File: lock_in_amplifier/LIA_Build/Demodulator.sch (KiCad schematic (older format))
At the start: 22 parts, among them J34 DEMOD PROG, J39 BOOT, J42 VOCM, J45 rst, J48 XOUT, U11 ADA2200, U5 LM833

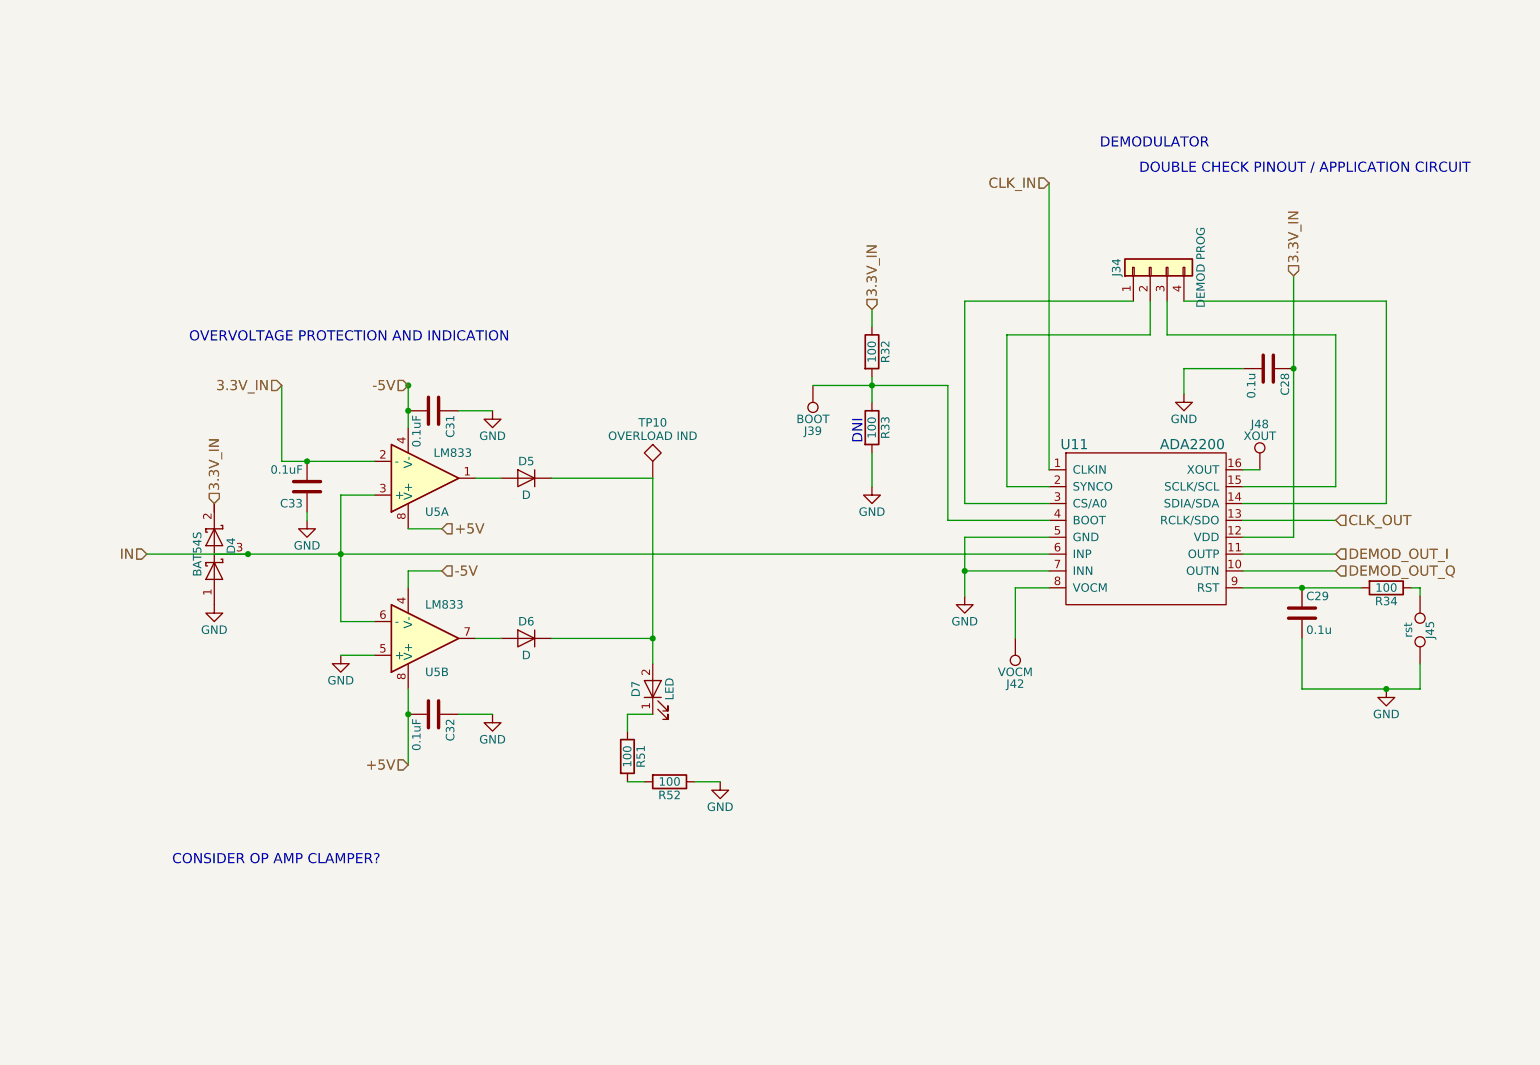
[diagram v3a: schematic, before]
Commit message: PLL initial implementation
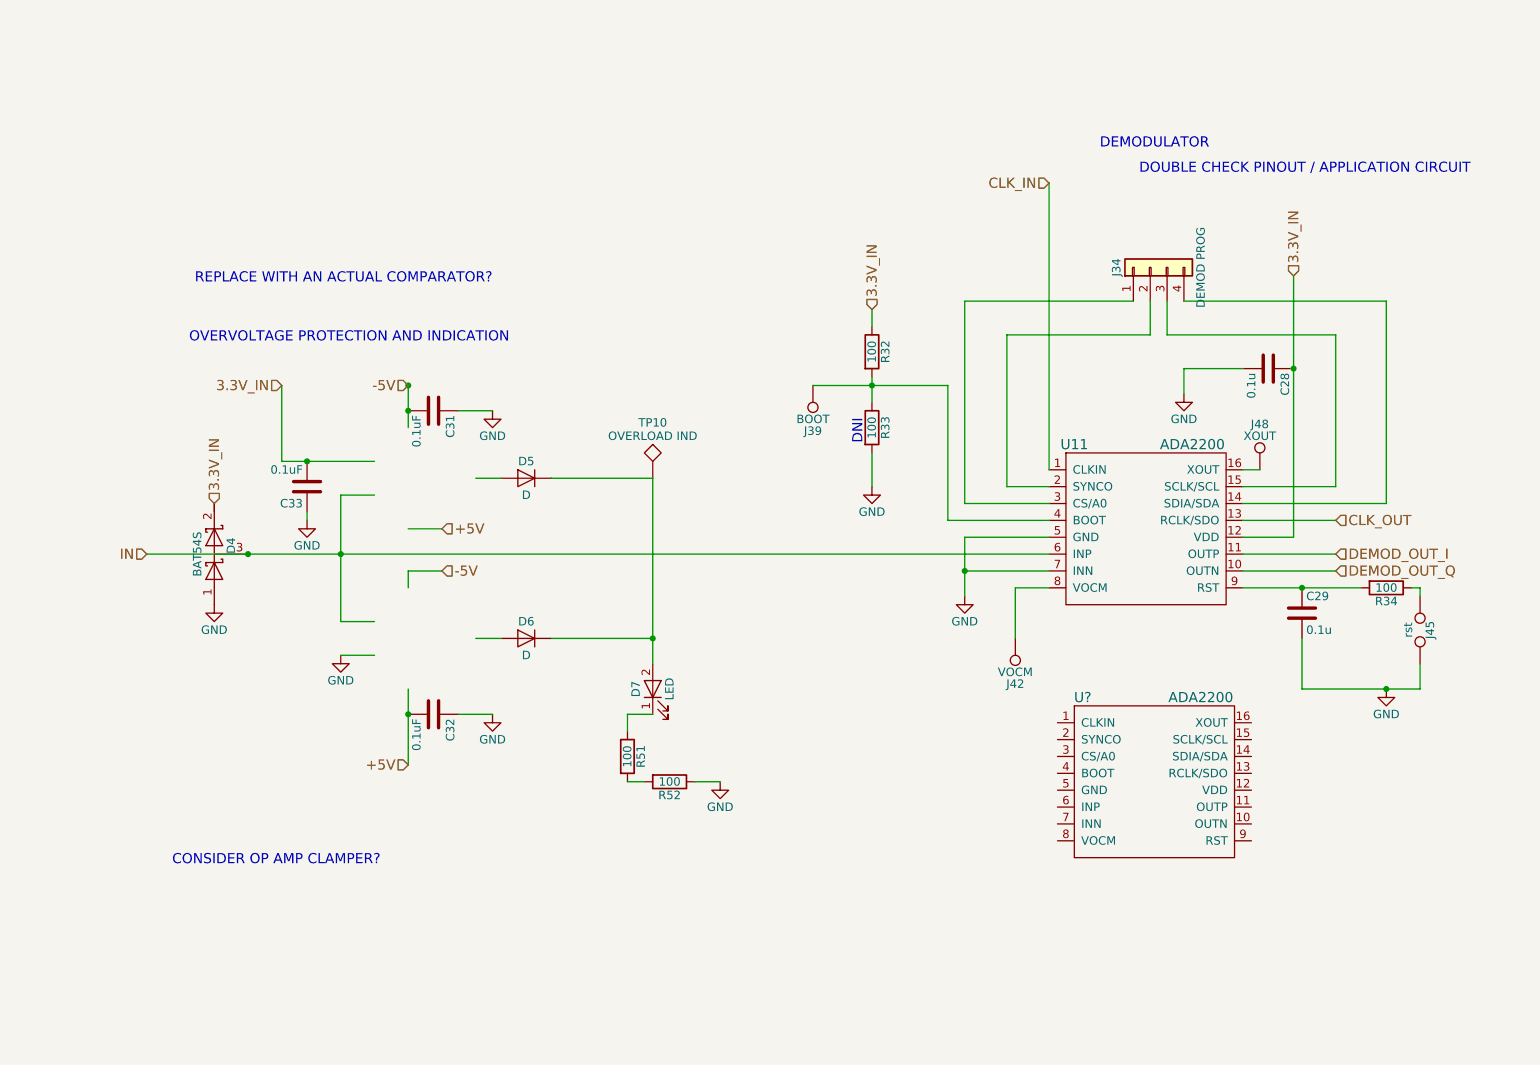
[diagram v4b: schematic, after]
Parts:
- removed U5: LM833, symbol LM358
- added U?: ADA2200, Housings_SSOP:TSSOP-20_4.4x6.5mm_Pitch0.65mm, symbol ADA2200
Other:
- note added: "REPLACE WITH AN ACTUAL COMPARATOR?"
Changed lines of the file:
@@
 $EndComp
 $Comp
-L GND #PWR045
+L GND #PWR50
 U 1 1 5A22E931
 P 6150 4200
-F 0 "#PWR045" H 6150 3950 50  0001 C CNN
+F 0 "#PWR50" H 6150 3950 50  0001 C CNN
 F 1 "GND" H 6150 4050 50  0000 C CNN
 F 2 "" H 6150 4200 50  0001 C CNN
@@
 $EndComp
 $Comp
-L GND #PWR046
+L GND #PWR51
 U 1 1 5A22EB23
 P 7450 3000
-F 0 "#PWR046" H 7450 2750 50  0001 C CNN
+F 0 "#PWR51" H 7450 2750 50  0001 C CNN
 F 1 "GND" H 7450 2850 50  0000 C CNN
 F 2 "" H 7450 3000 50  0001 C CNN
@@
 $EndComp
 $Comp
-L GND #PWR047
+L GND #PWR52
 U 1 1 5A22F9DC
 P 8650 4750
-F 0 "#PWR047" H 8650 4500 50  0001 C CNN
+F 0 "#PWR52" H 8650 4500 50  0001 C CNN
 F 1 "GND" H 8650 4600 50  0000 C CNN
 F 2 "" H 8650 4750 50  0001 C CNN
@@
 $EndComp
 $Comp
-L GND #PWR048
+L GND #PWR49
 U 1 1 5A22FE7B
 P 5600 3550
-F 0 "#PWR048" H 5600 3300 50  0001 C CNN
+F 0 "#PWR49" H 5600 3300 50  0001 C CNN
 F 1 "GND" H 5600 3400 50  0000 C CNN
 F 2 "" H 5600 3550 50  0001 C CNN
@@
 $EndComp
 $Comp
-L GND #PWR049
+L GND #PWR43
 U 1 1 5A231A02
 P 1700 4250
-F 0 "#PWR049" H 1700 4000 50  0001 C CNN
+F 0 "#PWR43" H 1700 4000 50  0001 C CNN
 F 1 "GND" H 1700 4100 50  0000 C CNN
 F 2 "" H 1700 4250 50  0001 C CNN
@@
 	0    -1   -1   0
 $EndComp
-$Comp
-L LM358 U5
-U 1 1 5A210395
-P 2950 3500
-F 0 "U5" H 2950 3700 50  0000 L CNN
-F 1 "LM833" H 3000 3350 50  0000 L CNN
-F 2 "" H 2950 3500 50  0001 C CNN
-F 3 "" H 2950 3500 50  0001 C CNN
-	1    2950 3500
-	1    0    0    1
-$EndComp
-$Comp
-L LM358 U5
-U 2 1 5A2103E8
-P 2950 4450
-F 0 "U5" H 2950 4650 50  0000 L CNN
-F 1 "LM833" H 2950 4250 50  0000 L CNN
-F 2 "" H 2950 4450 50  0001 C CNN
-F 3 "" H 2950 4450 50  0001 C CNN
-	2    2950 4450
-	1    0    0    1
-$EndComp
 Text HLabel 2100 2950 0    60   Input ~ 0
 3.3V_IN
 $Comp
-L GND #PWR050
+L GND #PWR45
 U 1 1 5A21049D
 P 2450 4550
-F 0 "#PWR050" H 2450 4300 50  0001 C CNN
+F 0 "#PWR45" H 2450 4300 50  0001 C CNN
 F 1 "GND" H 2450 4400 50  0000 C CNN
 F 2 "" H 2450 4550 50  0001 C CNN
@@
 Connection ~ 2450 3950
 $Comp
-L GND #PWR051
+L GND #PWR48
 U 1 1 5A2108F7
 P 4700 5300
-F 0 "#PWR051" H 4700 5050 50  0001 C CNN
+F 0 "#PWR48" H 4700 5050 50  0001 C CNN
 F 1 "GND" H 4700 5150 50  0000 C CNN
 F 2 "" H 4700 5300 50  0001 C CNN
@@
 $EndComp
 $Comp
-L GND #PWR052
+L GND #PWR46
 U 1 1 5A210C1D
 P 3350 3100
-F 0 "#PWR052" H 3350 2850 50  0001 C CNN
+F 0 "#PWR46" H 3350 2850 50  0001 C CNN
 F 1 "GND" H 3350 2950 50  0000 C CNN
 F 2 "" H 3350 3100 50  0001 C CNN
@@
 Connection ~ 2850 4900
 $Comp
-L GND #PWR053
+L GND #PWR47
 U 1 1 5A2111CA
 P 3350 4900
-F 0 "#PWR053" H 3350 4650 50  0001 C CNN
+F 0 "#PWR47" H 3350 4650 50  0001 C CNN
 F 1 "GND" H 3350 4750 50  0000 C CNN
 F 2 "" H 3350 4900 50  0001 C CNN
@@
 $EndComp
 $Comp
-L GND #PWR054
+L GND #PWR44
 U 1 1 5A214FCE
 P 2250 3750
-F 0 "#PWR054" H 2250 3500 50  0001 C CNN
+F 0 "#PWR44" H 2250 3500 50  0001 C CNN
 F 1 "GND" H 2250 3600 50  0000 C CNN
 F 2 "" H 2250 3750 50  0001 C CNN
@@
 Text Notes 1450 5800 0    60   ~ 0
 CONSIDER OP AMP CLAMPER?
+Text Notes 3350 2350 2    60   ~ 0
+REPLACE WITH AN ACTUAL COMPARATOR?
+$Comp
+L ADA2200 U?
+U 1 1 5A2936CF
+P 7250 5300
+F 0 "U?" H 6850 5800 60  0000 C CNN
+F 1 "ADA2200" H 7550 5800 60  0000 C CNN
+F 2 "Housings_SSOP:TSSOP-20_4.4x6.5mm_Pitch0.65mm" H 7150 5500 60  0001 C CNN
+F 3 "" H 7150 5500 60  0001 C CNN
+	1    7250 5300
+	1    0    0    -1
+$EndComp
 $EndSCHEMATC

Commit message: Added quadrature demod, phase shift to pll
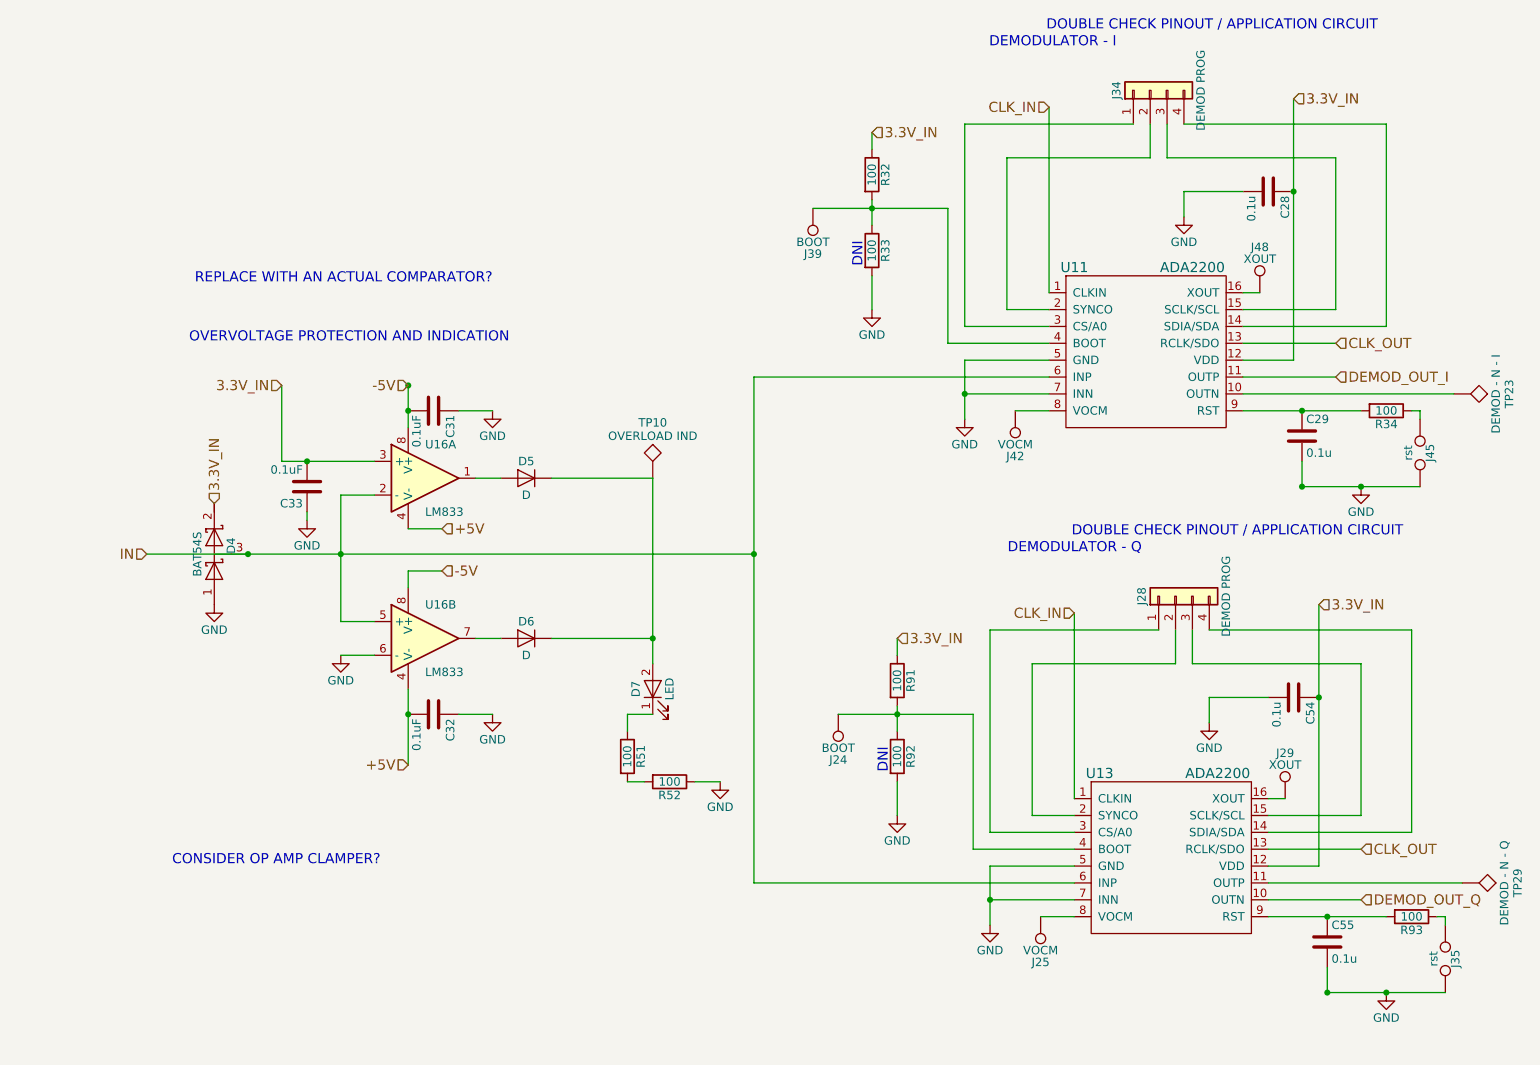
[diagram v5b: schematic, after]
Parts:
- removed U?: ADA2200, Housings_SSOP:TSSOP-20_4.4x6.5mm_Pitch0.65mm, symbol ADA2200
- added C54, C55: 0.1u, Capacitors_SMD:C_0805, symbol C
- added J24: BOOT, footprints:tyco_RCU_0603_Probe_Pad, symbol TEST_1P
- added J25: VOCM, footprints:tyco_RCU_0603_Probe_Pad, symbol TEST_1P
- added J28: DEMOD PROG, Pin_Headers:Pin_Header_Straight_1x04_Pitch2.54mm, symbol Conn_01x04
- added J29: XOUT, footprints:tyco_RCU_0603_Probe_Pad, symbol TEST_1P
- added J35: rst, symbol TEST_2P
- added R91, R92, R93: 100, Resistors_SMD:R_0805, symbol R
- added TP23: DEMOD - N - I, symbol TEST
- added TP29: DEMOD - N - Q, symbol TEST
- added U13: ADA2200, Housings_SSOP:TSSOP-20_4.4x6.5mm_Pitch0.65mm, symbol ADA2200
- added U16: LM833, symbol LM833
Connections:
- wire segments 64 -> 103
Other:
- note added: "DEMODULATOR - I"
- note added: "DEMODULATOR - Q"
- note removed: "DEMODULATOR"
- moved on the sheet: C28, C29, J34, J39, J42, J45, J48, R32, R33, R34, U11

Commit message: pll finalized - misc cleanup - review candidate
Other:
- note removed: "CONSIDER OP AMP CLAMPER?"
- note removed: "REPLACE WITH AN ACTUAL COMPARATOR?"
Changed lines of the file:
@@
 $EndComp
 $Comp
-L GND #PWR045
+L GND #PWR050
 U 1 1 5A22E931
 P 6150 3150
-F 0 "#PWR045" H 6150 2900 50  0001 C CNN
+F 0 "#PWR050" H 6150 2900 50  0001 C CNN
 F 1 "GND" H 6150 3000 50  0000 C CNN
 F 2 "" H 6150 3150 50  0001 C CNN
@@
 $EndComp
 $Comp
-L GND #PWR046
+L GND #PWR051
 U 1 1 5A22EB23
 P 7450 1950
-F 0 "#PWR046" H 7450 1700 50  0001 C CNN
+F 0 "#PWR051" H 7450 1700 50  0001 C CNN
 F 1 "GND" H 7450 1800 50  0000 C CNN
 F 2 "" H 7450 1950 50  0001 C CNN
@@
 $EndComp
 $Comp
-L GND #PWR047
+L GND #PWR052
 U 1 1 5A22F9DC
 P 8500 3550
-F 0 "#PWR047" H 8500 3300 50  0001 C CNN
+F 0 "#PWR052" H 8500 3300 50  0001 C CNN
 F 1 "GND" H 8500 3400 50  0000 C CNN
 F 2 "" H 8500 3550 50  0001 C CNN
@@
 $EndComp
 $Comp
-L GND #PWR048
+L GND #PWR053
 U 1 1 5A22FE7B
 P 5600 2500
-F 0 "#PWR048" H 5600 2250 50  0001 C CNN
+F 0 "#PWR053" H 5600 2250 50  0001 C CNN
 F 1 "GND" H 5600 2350 50  0000 C CNN
 F 2 "" H 5600 2500 50  0001 C CNN
@@
 $EndComp
 $Comp
-L GND #PWR049
+L GND #PWR054
 U 1 1 5A231A02
 P 1700 4250
-F 0 "#PWR049" H 1700 4000 50  0001 C CNN
+F 0 "#PWR054" H 1700 4000 50  0001 C CNN
 F 1 "GND" H 1700 4100 50  0000 C CNN
 F 2 "" H 1700 4250 50  0001 C CNN
@@
 3.3V_IN
 $Comp
-L GND #PWR050
+L GND #PWR055
 U 1 1 5A21049D
 P 2450 4550
-F 0 "#PWR050" H 2450 4300 50  0001 C CNN
+F 0 "#PWR055" H 2450 4300 50  0001 C CNN
 F 1 "GND" H 2450 4400 50  0000 C CNN
 F 2 "" H 2450 4550 50  0001 C CNN
@@
 Connection ~ 2450 3950
 $Comp
-L GND #PWR051
+L GND #PWR056
 U 1 1 5A2108F7
 P 4700 5300
-F 0 "#PWR051" H 4700 5050 50  0001 C CNN
+F 0 "#PWR056" H 4700 5050 50  0001 C CNN
 F 1 "GND" H 4700 5150 50  0000 C CNN
 F 2 "" H 4700 5300 50  0001 C CNN
@@
 $EndComp
 $Comp
-L GND #PWR052
+L GND #PWR057
 U 1 1 5A210C1D
 P 3350 3100
-F 0 "#PWR052" H 3350 2850 50  0001 C CNN
+F 0 "#PWR057" H 3350 2850 50  0001 C CNN
 F 1 "GND" H 3350 2950 50  0000 C CNN
 F 2 "" H 3350 3100 50  0001 C CNN
@@
 Connection ~ 2850 4900
 $Comp
-L GND #PWR053
+L GND #PWR058
 U 1 1 5A2111CA
 P 3350 4900
-F 0 "#PWR053" H 3350 4650 50  0001 C CNN
+F 0 "#PWR058" H 3350 4650 50  0001 C CNN
 F 1 "GND" H 3350 4750 50  0000 C CNN
 F 2 "" H 3350 4900 50  0001 C CNN
@@
 $EndComp
 $Comp
-L GND #PWR054
+L GND #PWR059
 U 1 1 5A214FCE
 P 2250 3750
-F 0 "#PWR054" H 2250 3500 50  0001 C CNN
+F 0 "#PWR059" H 2250 3500 50  0001 C CNN
 F 1 "GND" H 2250 3600 50  0000 C CNN
 F 2 "" H 2250 3750 50  0001 C CNN
@@
 	1    0    0    -1
 $EndComp
-Text Notes 1450 5800 0    60   ~ 0
-CONSIDER OP AMP CLAMPER?
-Text Notes 3350 2350 2    60   ~ 0
-REPLACE WITH AN ACTUAL COMPARATOR?
 Wire Wire Line
 	8150 3550 8850 3550
@@
 $EndComp
 $Comp
-L GND #PWR055
+L GND #PWR060
 U 1 1 5A28BA97
 P 6300 6150
-F 0 "#PWR055" H 6300 5900 50  0001 C CNN
+F 0 "#PWR060" H 6300 5900 50  0001 C CNN
 F 1 "GND" H 6300 6000 50  0000 C CNN
 F 2 "" H 6300 6150 50  0001 C CNN
@@
 $EndComp
 $Comp
-L GND #PWR056
+L GND #PWR061
 U 1 1 5A28BA9D
 P 7600 4950
-F 0 "#PWR056" H 7600 4700 50  0001 C CNN
+F 0 "#PWR061" H 7600 4700 50  0001 C CNN
 F 1 "GND" H 7600 4800 50  0000 C CNN
 F 2 "" H 7600 4950 50  0001 C CNN
@@
 $EndComp
 $Comp
-L GND #PWR057
+L GND #PWR062
 U 1 1 5A28BABC
 P 8650 6550
-F 0 "#PWR057" H 8650 6300 50  0001 C CNN
+F 0 "#PWR062" H 8650 6300 50  0001 C CNN
 F 1 "GND" H 8650 6400 50  0000 C CNN
 F 2 "" H 8650 6550 50  0001 C CNN
@@
 $EndComp
 $Comp
-L GND #PWR058
+L GND #PWR063
 U 1 1 5A28BACE
 P 5750 5500
-F 0 "#PWR058" H 5750 5250 50  0001 C CNN
+F 0 "#PWR063" H 5750 5250 50  0001 C CNN
 F 1 "GND" H 5750 5350 50  0000 C CNN
 F 2 "" H 5750 5500 50  0001 C CNN
@@
 	-1   0    0    1
 $EndComp
-Text Notes 8750 3850 2    60   ~ 0
-DOUBLE CHECK PINOUT / APPLICATION CIRCUIT
 Text Notes 7200 3950 2    60   ~ 0
 DEMODULATOR - Q
@@
 	1    0    0    -1
 $EndComp
+$Comp
+L PWR_FLAG #FLG064
+U 1 1 5A2D24A6
+P 8250 4250
+F 0 "#FLG064" H 8250 4325 50  0001 C CNN
+F 1 "PWR_FLAG" H 8250 4400 50  0000 C CNN
+F 2 "" H 8250 4250 50  0001 C CNN
+F 3 "" H 8250 4250 50  0001 C CNN
+	1    8250 4250
+	1    0    0    -1
+$EndComp

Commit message: started LNA test board.
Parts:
- C31, C32, C33: footprint (none) -> Capacitors_SMD:C_0805
- D5, D6: footprint (none) -> Diodes_SMD:D_0805
- D7: footprint (none) -> LEDs:LED_0805
- J35, J45: footprint (none) -> Pin_Headers:Pin_Header_Straight_1x02_Pitch2.54mm
- R51, R52: footprint (none) -> Resistors_SMD:R_0805
- TP10, TP23, TP29: footprint (none) -> footprints:tyco_RCU_0603_Probe_Pad
- U16: footprint (none) -> Housings_SOIC:SO-8_5.3x6.2mm_Pitch1.27mm
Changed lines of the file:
@@
 F 0 "J45" H 8850 3410 50  0000 C CNN
 F 1 "rst" H 8850 3280 50  0000 C CNN
-F 2 "" H 8850 3350 50  0001 C CNN
+F 2 "Pin_Headers:Pin_Header_Straight_1x02_Pitch2.54mm" H 8850 3350 50  0001 C CNN
 F 3 "" H 8850 3350 50  0001 C CNN
 	1    8850 3350
@@
 F 0 "D5" H 3550 3600 50  0000 C CNN
 F 1 "D" H 3550 3400 50  0000 C CNN
-F 2 "" H 3550 3500 50  0001 C CNN
+F 2 "Diodes_SMD:D_0805" H 3550 3500 50  0001 C CNN
 F 3 "" H 3550 3500 50  0001 C CNN
 	1    3550 3500
@@
 F 0 "D6" H 3550 4550 50  0000 C CNN
 F 1 "D" H 3550 4350 50  0000 C CNN
-F 2 "" H 3550 4450 50  0001 C CNN
+F 2 "Diodes_SMD:D_0805" H 3550 4450 50  0001 C CNN
 F 3 "" H 3550 4450 50  0001 C CNN
 	1    3550 4450
@@
 F 0 "D7" H 4300 4850 50  0000 C CNN
 F 1 "LED" H 4300 4650 50  0000 C CNN
-F 2 "" H 4300 4750 50  0001 C CNN
+F 2 "LEDs:LED_0805" H 4300 4750 50  0001 C CNN
 F 3 "" H 4300 4750 50  0001 C CNN
 	1    4300 4750
@@
 F 0 "C31" H 3025 3200 50  0000 L CNN
 F 1 "0.1uF" H 3025 3000 50  0000 L CNN
-F 2 "" H 3038 2950 50  0001 C CNN
+F 2 "Capacitors_SMD:C_0805" H 3038 2950 50  0001 C CNN
 F 3 "" H 3000 3100 50  0001 C CNN
 	1    3000 3100
@@
 F 0 "C32" H 3025 5000 50  0000 L CNN
 F 1 "0.1uF" H 3025 4800 50  0000 L CNN
-F 2 "" H 3038 4750 50  0001 C CNN
+F 2 "Capacitors_SMD:C_0805" H 3038 4750 50  0001 C CNN
 F 3 "" H 3000 4900 50  0001 C CNN
 	1    3000 4900
@@
 F 0 "R51" V 4230 5150 50  0000 C CNN
 F 1 "100" V 4150 5150 50  0000 C CNN
-F 2 "" V 4080 5150 50  0001 C CNN
+F 2 "Resistors_SMD:R_0805" V 4080 5150 50  0001 C CNN
 F 3 "" H 4150 5150 50  0001 C CNN
 	1    4150 5150
@@
 F 0 "R52" V 4480 5300 50  0000 C CNN
 F 1 "100" V 4400 5300 50  0000 C CNN
-F 2 "" V 4330 5300 50  0001 C CNN
+F 2 "Resistors_SMD:R_0805" V 4330 5300 50  0001 C CNN
 F 3 "" H 4400 5300 50  0001 C CNN
 	1    4400 5300
@@
 F 0 "C33" H 2275 3650 50  0000 L CNN
 F 1 "0.1uF" H 2275 3450 50  0000 L CNN
-F 2 "" H 2288 3400 50  0001 C CNN
+F 2 "Capacitors_SMD:C_0805" H 2288 3400 50  0001 C CNN
 F 3 "" H 2250 3550 50  0001 C CNN
 	1    2250 3550
@@
 F 0 "TP10" H 4300 3800 50  0000 C BNN
 F 1 "OVERLOAD IND" H 4300 3750 50  0000 C CNN
-F 2 "" H 4300 3500 50  0001 C CNN
+F 2 "footprints:tyco_RCU_0603_Probe_Pad" H 4300 3500 50  0001 C CNN
 F 3 "" H 4300 3500 50  0001 C CNN
 	1    4300 3500
@@
 F 0 "J35" H 9000 6410 50  0000 C CNN
 F 1 "rst" H 9000 6280 50  0000 C CNN
-F 2 "" H 9000 6350 50  0001 C CNN
+F 2 "Pin_Headers:Pin_Header_Straight_1x02_Pitch2.54mm" H 9000 6350 50  0001 C CNN
 F 3 "" H 9000 6350 50  0001 C CNN
 	1    9000 6350
@@
 F 0 "TP23" H 9050 3300 50  0000 C BNN
 F 1 "DEMOD - N - I" H 9050 3250 50  0000 C CNN
-F 2 "" H 9050 3000 50  0001 C CNN
+F 2 "footprints:tyco_RCU_0603_Probe_Pad" H 9050 3000 50  0001 C CNN
 F 3 "" H 9050 3000 50  0001 C CNN
 	1    9050 3000
@@
 F 0 "TP29" H 9100 6200 50  0000 C BNN
 F 1 "DEMOD - N - Q" H 9100 6150 50  0000 C CNN
-F 2 "" H 9100 5900 50  0001 C CNN
+F 2 "footprints:tyco_RCU_0603_Probe_Pad" H 9100 5900 50  0001 C CNN
 F 3 "" H 9100 5900 50  0001 C CNN
 	1    9100 5900
@@
 F 0 "U16" H 2950 3700 50  0000 L CNN
 F 1 "LM833" H 2950 3300 50  0000 L CNN
-F 2 "" H 2950 3500 50  0001 C CNN
+F 2 "Housings_SOIC:SO-8_5.3x6.2mm_Pitch1.27mm" H 2950 3500 50  0001 C CNN
 F 3 "" H 2950 3500 50  0001 C CNN
 	1    2950 3500
@@
 F 0 "U16" H 2950 4650 50  0000 L CNN
 F 1 "LM833" H 2950 4250 50  0000 L CNN
-F 2 "" H 2950 4450 50  0001 C CNN
+F 2 "Housings_SOIC:SO-8_5.3x6.2mm_Pitch1.27mm" H 2950 4450 50  0001 C CNN
 F 3 "" H 2950 4450 50  0001 C CNN
 	2    2950 4450
